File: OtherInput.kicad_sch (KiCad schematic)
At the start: 22 parts, among them SW1301 SW_SPST_LED, SW1302 SW_SPST_LED, SW1303 SW_SPST_LED, SW1304 Encoder

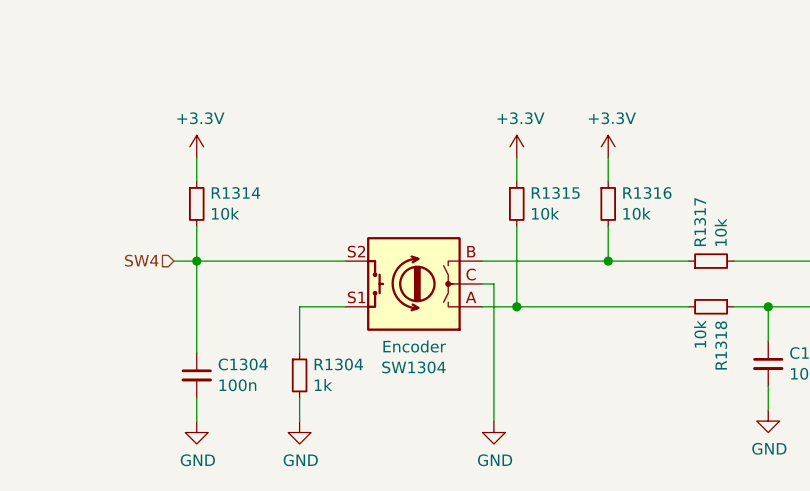
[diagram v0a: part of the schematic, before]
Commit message: Update to KiCad 6
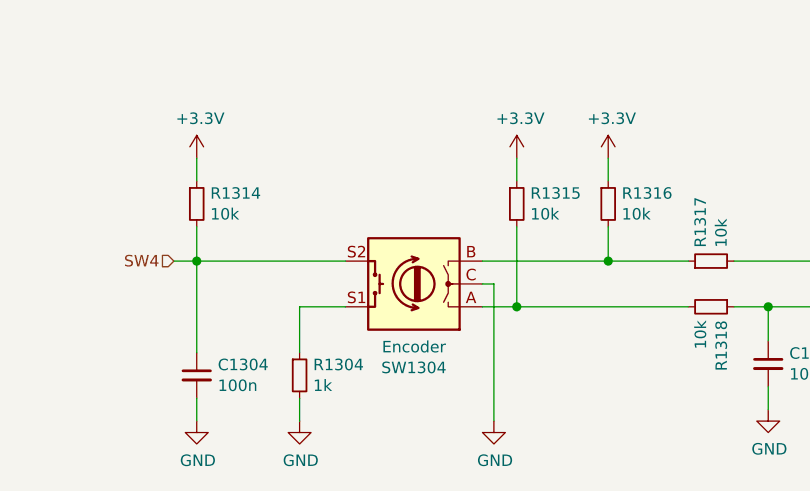
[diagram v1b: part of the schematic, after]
